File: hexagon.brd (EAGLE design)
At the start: 50 x 43.3 mm, 27 parts, among them J1 AVR_SPI_PROG_3X22X3_LOCK, U1 ATMEGA328P_TQFP, Y2 16Mhz, Y2B 16MHz

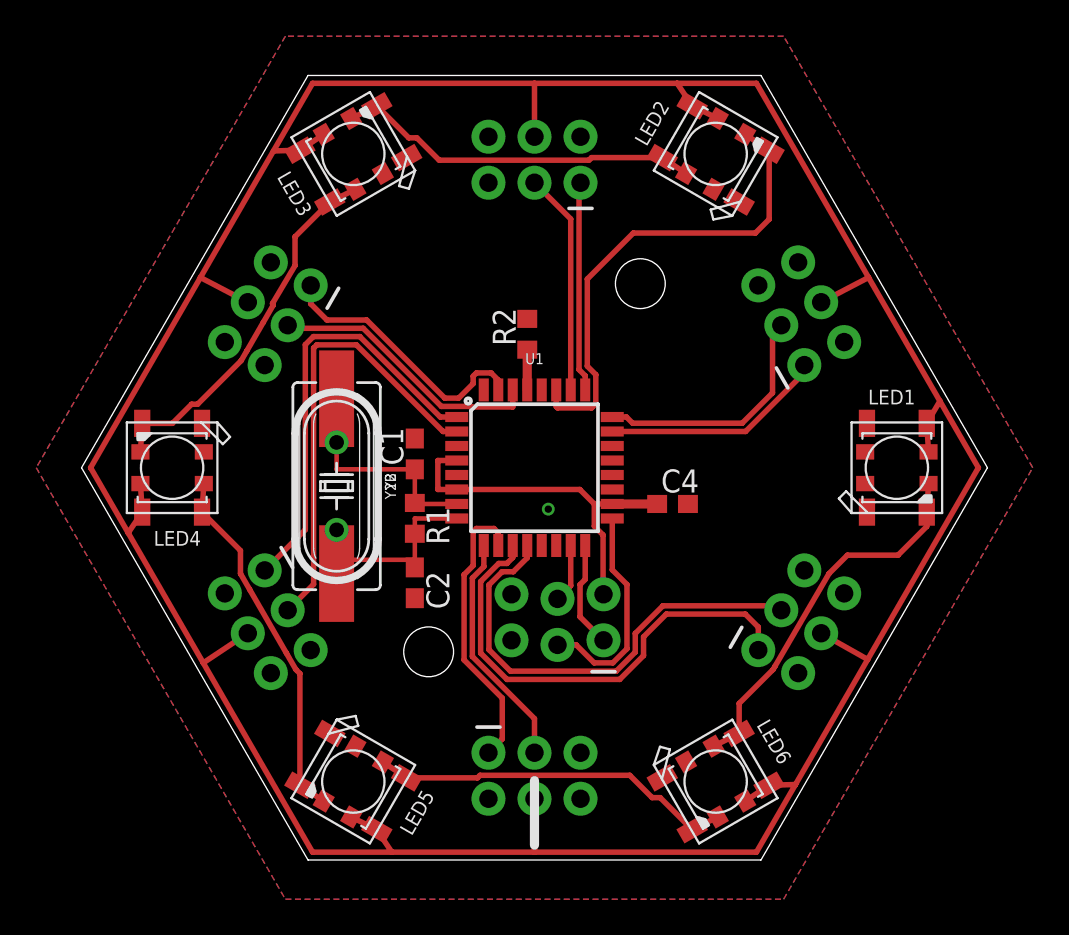
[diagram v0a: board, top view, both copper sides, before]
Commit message: Continuing to work out the layout kinks. Added ESP.
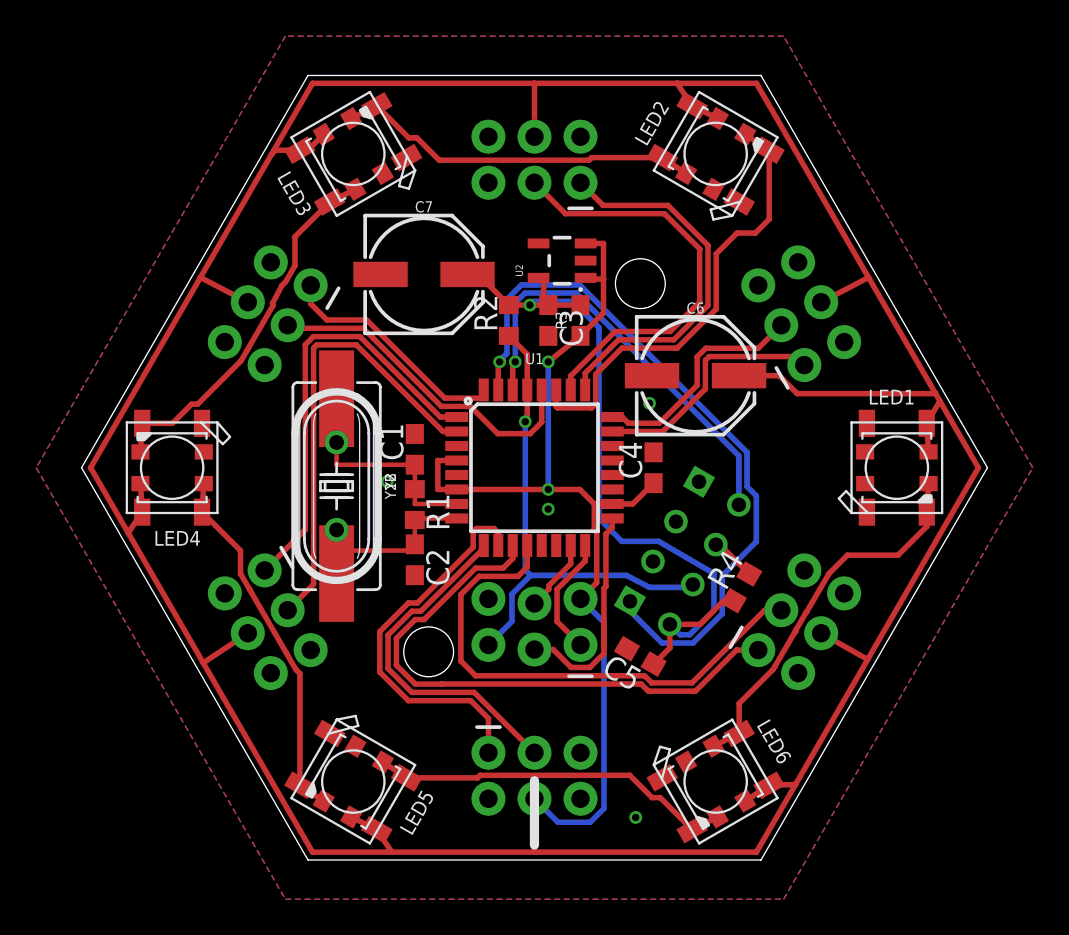
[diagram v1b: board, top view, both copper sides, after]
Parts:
- added C3, C5: 0.1uF, rcl:C0603
- added C6, C7: 47uF, SparkFun-Capacitors:PANASONIC_D
- added R3: 0 Ohm NC, SparkFun-Resistors:0603
- added R4: 10k, rcl:R0603
- added U$1: ESP01, esp8266modules:ESP01
- added U2: 3.3V, SparkFun-IC-Power:SOT23-5
- moved C4 2.26 mm to (6.57, 0.00), turned to 90 degrees
- moved J1 1.30 mm to (2.54, -9.91)
- moved R2 1.27 mm to (-1.42, 8.13)
- moved C2 1.27 mm to (-6.60, -5.08)
- moved R1 0.76 mm to (-6.60, -2.03)
- moved C1 0.25 mm to (-6.60, 1.02)
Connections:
- removed net IO2: U1.32
- new net 3.3V: C3.1, C5.1, C7.+, R2.2, R3.2, R4.1, U$1.VCC, U2.5
- new net ATRX_ETX: U$1.TX, U1.30
- new net ATTX_ERX: U$1.RX, U1.31
- new net N$2: R4.2, U$1.CH_PD
- net +5V: now also C6.+, R3.1, U2.1, U2.3; no longer R2.2
- net GND: now also C3.2, C5.2, C6.-, C7.-, U$1.GND, U2.2
- net M3_RX: now also U1.28; no longer U1.30
- net M3_TX: now also U1.32; no longer U1.31
- net RESET: now also U$1.RST
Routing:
- net +5V: track 203.2 -> 249.4 mm, vias 0 -> 2
- net 3.3V: track 0.00 -> 43.1 mm, vias 0 -> 1
- net ATTX_ERX: track 0.00 -> 39.5 mm, vias 0 -> 1
- net RESET: track 2.22 -> 27.8 mm, vias 0 -> 1
- net ATRX_ETX: track 0.00 -> 23.9 mm, vias 0 -> 1
- net M2_RX: track 12.3 -> 23.2 mm
- net M2_TX: track 11.6 -> 21.0 mm
- net M5_RX: track 13.1 -> 19.3 mm
- net M5_TX: track 15.9 -> 21.4 mm
- net M6_TX: track 26.5 -> 32.0 mm
- net M3_RX: track 15.2 -> 18.5 mm
- net M6_RX: track 25.8 -> 29.0 mm
- net N$2: track 0.00 -> 2.52 mm
- net STRAND_IN: track 27.3 -> 25.3 mm
- net M3_TX: track 15.1 -> 13.2 mm
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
